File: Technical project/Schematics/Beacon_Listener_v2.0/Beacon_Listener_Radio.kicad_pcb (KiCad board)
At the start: 2 copper layers, 60 x 60 mm, 33 parts, among them J1 Conn_01x06_Female, J2 input AC, J3 select if usb or AC power, J4 USB_B_Micro, J5 Conn_01x03_Male, J6 Conn_01x03_Male, J7 Conn_Coaxial, SW1 SW_Push, SW2 SW_Push, U1 ESP32-WROVER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

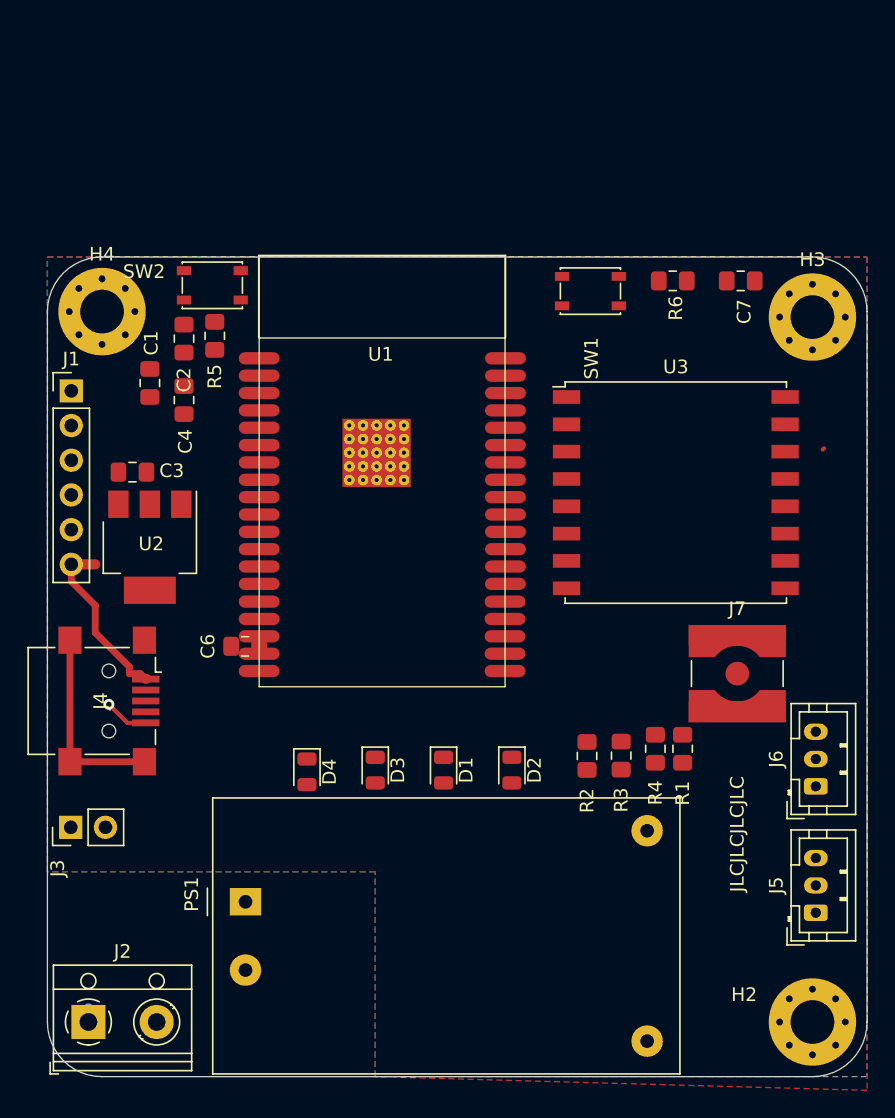
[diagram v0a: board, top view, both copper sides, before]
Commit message: rf95 module
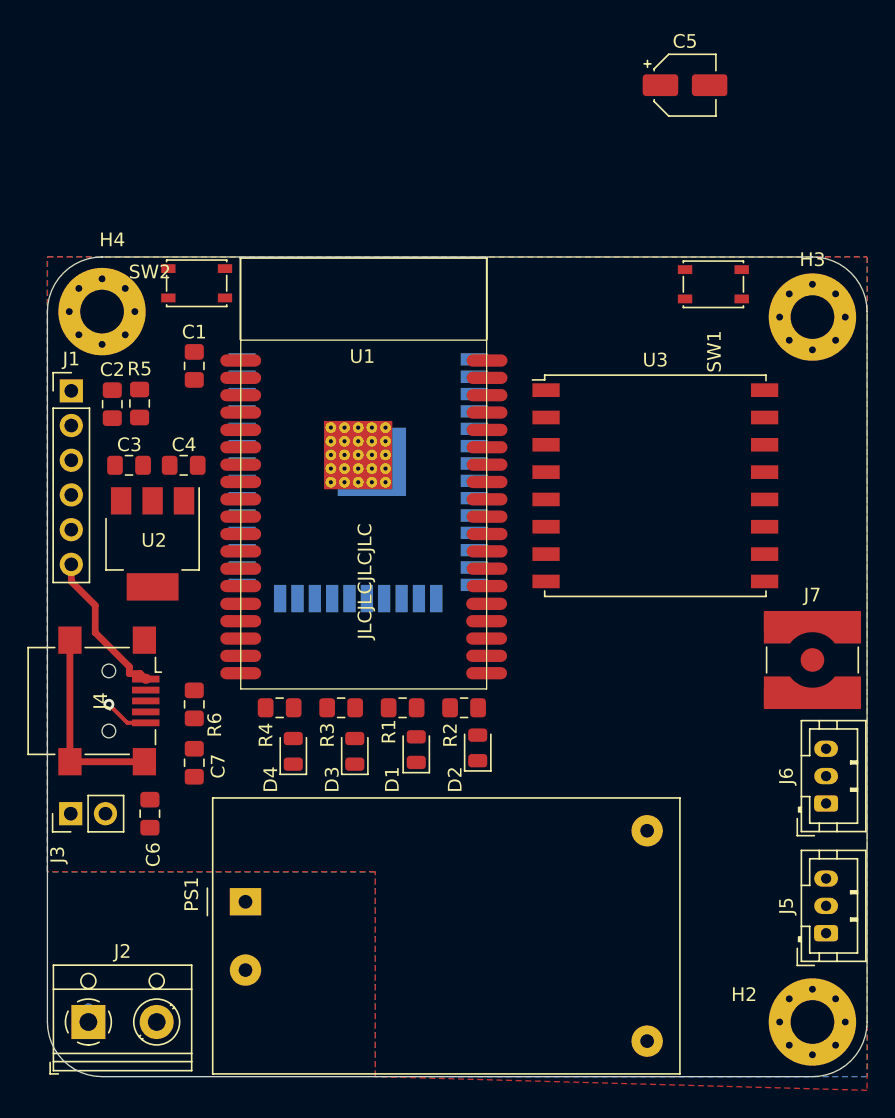
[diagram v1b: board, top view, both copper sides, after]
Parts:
- added C5: 10u, Capacitor_SMD:CP_Elec_4x5.3, F.Cu at (133.7, 56.4)
- added U4: ESP32-WROOM-32, RF_Module:ESP32-WROOM-32, B.Cu at (109.8, 84.8)
- moved C7 53.3 mm to (97.8, 106.0), turned to 270 degrees
- moved R6 46.8 mm to (97.8, 101.8), turned to 270 degrees
- moved R4 27.7 mm to (104.0, 102.0), turned to 0 degrees
- moved R3 20.8 mm to (108.5, 102.0), turned to 0 degrees
- moved R1 20.7 mm to (113.0, 102.0), turned to 0 degrees
- moved C6 14.1 mm to (94.5, 109.8), turned to 270 degrees
- moved R2 9.67 mm to (117.5, 102.0), turned to 0 degrees
- moved SW1 9.01 mm to (135.8, 71.0)
- moved R5 7.40 mm to (93.8, 79.7), turned to 270 degrees
- moved C2 7.11 mm to (91.8, 79.8), turned to 90 degrees
- moved J7 5.59 mm to (143.0, 98.5)
- moved C4 4.78 mm to (97.0, 84.2), turned to 180 degrees
- moved C1 3.48 mm to (97.8, 77.0)
- moved D2 2.98 mm to (118.5, 104.9), turned to 90 degrees
- moved D1 2.50 mm to (114.0, 105.1), turned to 90 degrees
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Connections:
- U3 pad 1: GND -> Net-(U3-Pad1)
- U3 pad 10: GND -> Net-(U3-Pad1)
- U3 pad 8: GND -> Net-(U3-Pad1)
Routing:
- net +5V: track 12.9 -> 11.2 mm

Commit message: radio module include on the 2 version of pcb
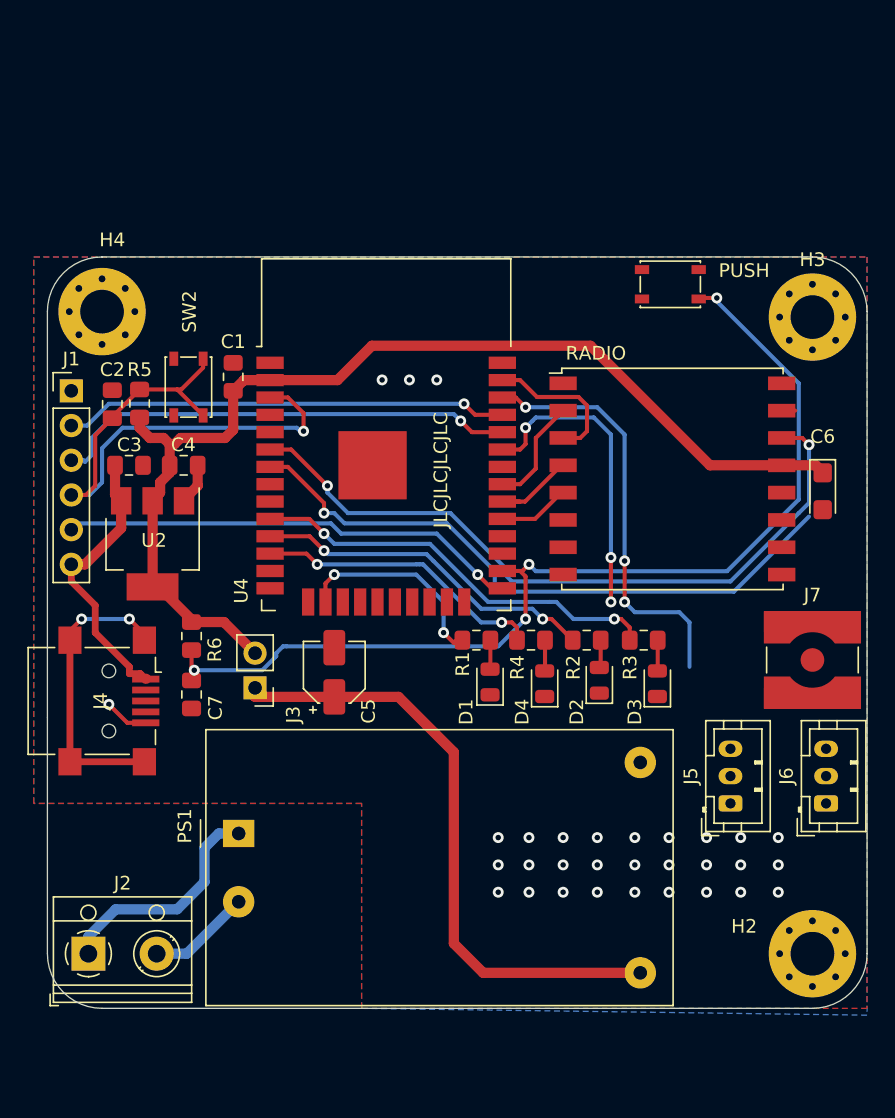
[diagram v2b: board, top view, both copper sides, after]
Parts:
- removed U1: ESP32-WROVER, ESP_32_all:ESP32-WROVER
- C6: value 10u -> CP; footprint Capacitor_SMD:C_0805_2012Metric_Pad1.15x1.40mm_HandSolder -> Capacitor_Tantalum_SMD:CP_EIA-3216-10_Kemet-I
- U4: moved to F.Cu
- moved C6 54.6 mm to (143.8, 86.2)
- moved C5 50.1 mm to (108.0, 99.4), turned to 90 degrees
- moved D3 22.7 mm to (131.7, 100.2)
- moved R3 22.7 mm to (130.7, 97.0)
- moved D4 19.1 mm to (123.4, 100.2)
- moved R4 19.1 mm to (122.4, 97.0)
- moved J3 16.3 mm to (102.2, 100.5), turned to 180 degrees
- moved J5 11.8 mm to (137.0, 109.0)
- moved R2 10.2 mm to (126.5, 97.0)
- moved D2 10.2 mm to (127.4, 100.0)
- moved SW2 7.62 mm to (97.3, 78.5), turned to 270 degrees
- moved D1 7.33 mm to (119.4, 100.1)
- moved R1 7.33 mm to (118.4, 97.0)
- moved PS1 5.02 mm to (101.0, 111.2)
- moved C7 5.00 mm to (97.5, 101.0)
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- renumbered SW1 to PUSH, U3 to RADIO
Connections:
- C6 pad 1: MainInput -> +3V3
- RADIO pad 1: Net-(U3-Pad1) -> GND
- RADIO pad 10: Net-(U3-Pad1) -> GND
- RADIO pad 8: Net-(U3-Pad1) -> GND
- U4 pad 27: TX_UART2 -> RX_UART2
- U4 pad 28: RX_UART2 -> TX_UART2
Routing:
- net +3V3: track 0.00 -> 80.4 mm
- net ConfigButton: track 0.00 -> 74.9 mm, vias 0 -> 4
- net RF_INT: track 0.00 -> 52.9 mm, vias 0 -> 2
- net INT_CAD: track 0.00 -> 47.5 mm, vias 0 -> 1
- net MainInput: track 0.00 -> 45.4 mm
- net EN: track 0.00 -> 44.0 mm, vias 0 -> 1
- net RX: track 0.00 -> 34.3 mm, vias 0 -> 1
- net GPIO0: track 0.00 -> 33.7 mm, vias 0 -> 1
- net TX: track 0.00 -> 32.5 mm, vias 0 -> 1
- net SCL: track 0.00 -> 30.9 mm, vias 0 -> 3
- net LED3: track 0.00 -> 30.5 mm, vias 0 -> 2
- net LED2: track 0.00 -> 25.3 mm, vias 0 -> 2
- net SDA: track 0.00 -> 22.4 mm, vias 0 -> 3
- net LED4: track 0.00 -> 21.2 mm, vias 0 -> 2
- net AC: track 1.00 -> 16.8 mm
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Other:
- board size 60 x 60 mm -> 60 x 55 mm
